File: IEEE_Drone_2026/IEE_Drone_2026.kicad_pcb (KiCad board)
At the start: 4 copper layers, 49 x 49.5 mm, 48 parts, among them IC1 TPSM84209RKHT, J1 ESC, J10 M2, J12 RF, J13 USB_C_Receptacle_USB2.0_16P, J2 M4 Mounting, J3 M4 Mounting, J4 M4 Mounting, J5 M4 Mounting, J6 Pixy2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

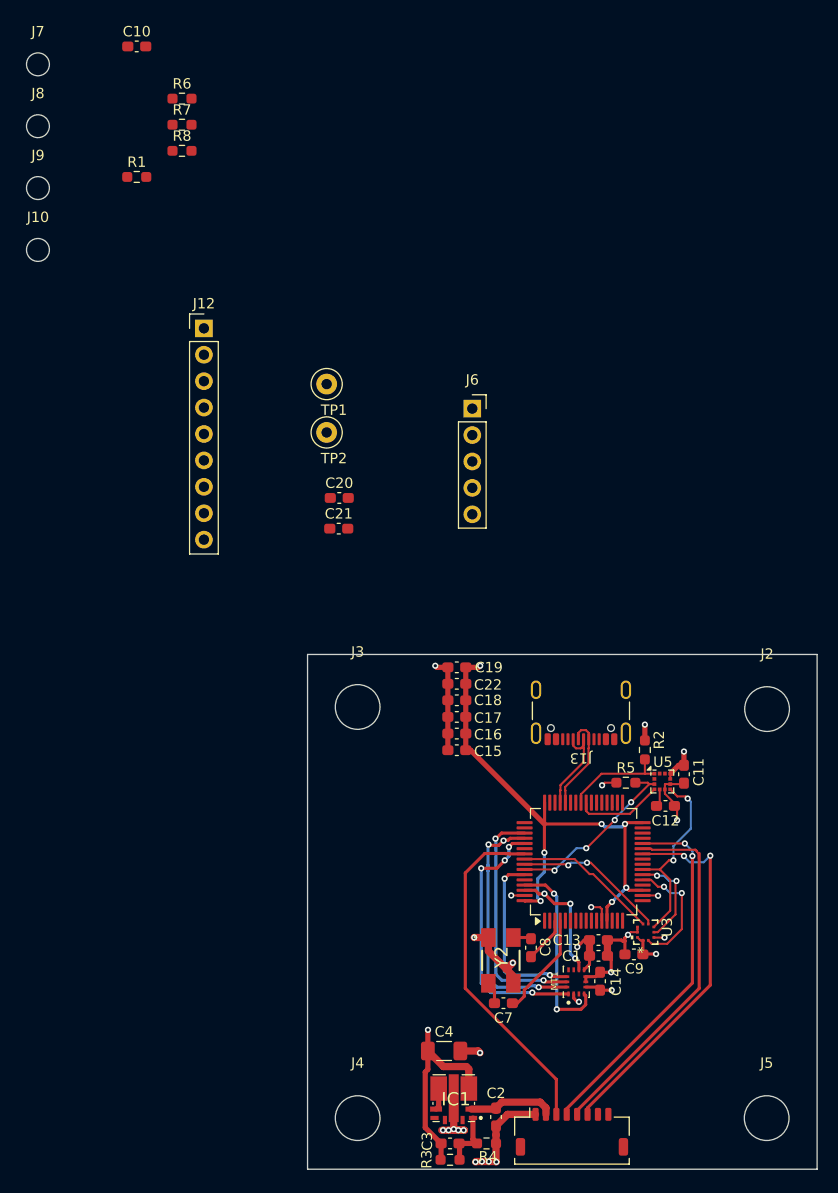
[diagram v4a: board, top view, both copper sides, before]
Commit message: updated lots
finished board internals routing, starting schematic routing for the gps, rf, and pixy
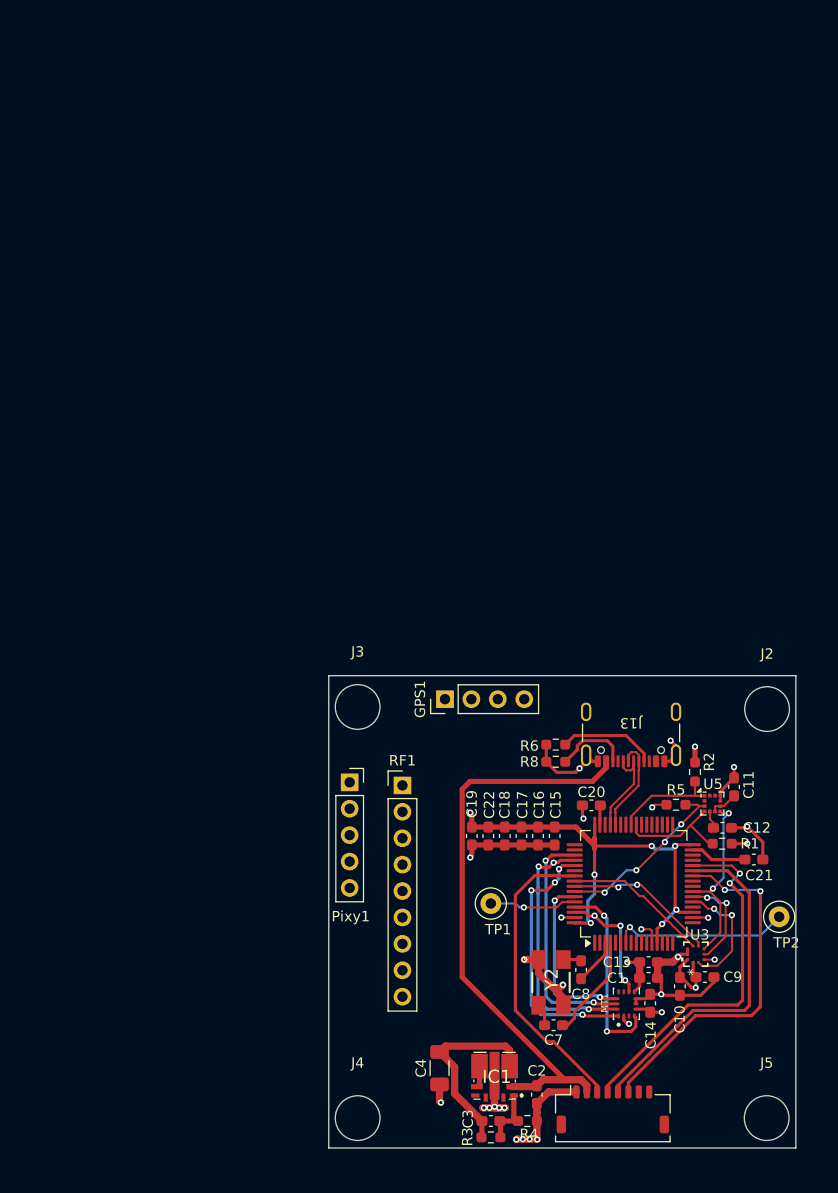
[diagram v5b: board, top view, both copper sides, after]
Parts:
- removed J10, J7, J8, J9: M2, MountingHole:MountingHole_2.2mm_M2
- removed R7: 300, Resistor_SMD:R_0603_1608Metric_Pad0.98x0.95mm_HandSolder
- added GPS1: GPS, Connector_PinHeader_2.54mm:PinHeader_1x04_P2.54mm_Vertical, F.Cu at (76.2, 85.8)
- moved C10 104.4 mm to (98.8, 113.4), turned to -90 degrees
- moved R1 85.3 mm to (102.9, 99.7), turned to 180 degrees
- moved R6 71.8 mm to (86.9, 90.2)
- moved R8 68.9 mm to (86.9, 91.8)
- moved TP2 63.7 mm to (108.3, 106.7)
- moved TP1 52.4 mm to (80.6, 105.5)
- moved C21 51.0 mm to (105.9, 101.2)
- moved RF1 47.9 mm to (72.1, 94.1)
- moved C20 38.2 mm to (90.3, 96.0), turned to 180 degrees
- moved Pixy1 37.8 mm to (67.0, 93.8)
- moved C19 16.3 mm to (78.8, 99.0), turned to -90 degrees
- moved C22 14.9 mm to (80.4, 99.0), turned to -90 degrees
- moved C18 13.8 mm to (82.0, 99.0), turned to -90 degrees
- moved C17 13.0 mm to (83.6, 99.0), turned to -90 degrees
- moved C16 12.6 mm to (85.2, 99.0), turned to -90 degrees
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- renumbered J6 to Pixy1, J12 to RF1
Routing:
- net +VDC: track 8.40 -> 55.6 mm
- net GND: track 58.3 -> 77.8 mm, vias 21 -> 24
- net Net-(U2-NRST): track 0.00 -> 17.1 mm, vias 0 -> 1
- net Net-(J13-CC1): track 0.00 -> 9.41 mm
- net Net-(U2-BOOT0): track 0.00 -> 8.44 mm, vias 0 -> 1
- net Net-(J13-CC2): track 0.00 -> 7.30 mm
- net Net-(U2-VCAP_1): track 0.00 -> 5.40 mm
- net /PB3: track 44.4 -> 40.1 mm
- net /SDA (I2C3): track 8.45 -> 11.3 mm
- net /PB1: track 36.1 -> 33.6 mm
- net Net-(U2-VCAP_2): track 0.00 -> 1.88 mm
- net /PB0: track 36.9 -> 35.3 mm
- net /MOSI: track 18.7 -> 17.4 mm
- net +3.3V: track 89.5 -> 88.3 mm
- net /PB2: track 35.5 -> 35.0 mm
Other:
- board size 49 x 49.5 mm -> 44.9 x 45.4 mm

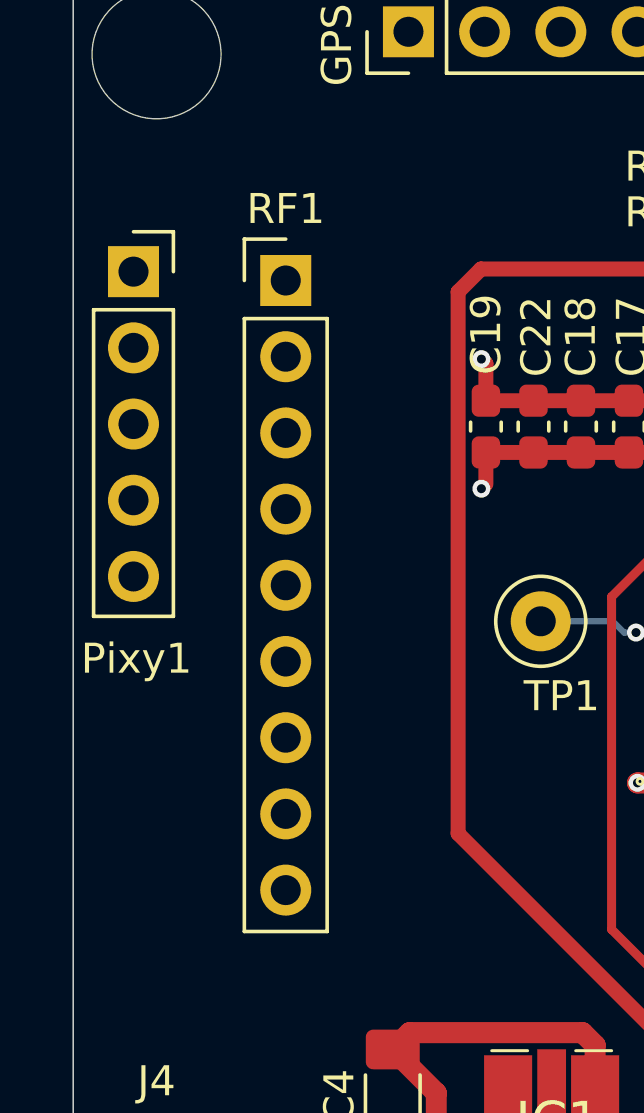
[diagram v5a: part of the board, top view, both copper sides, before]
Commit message: finished schematic connections for pins
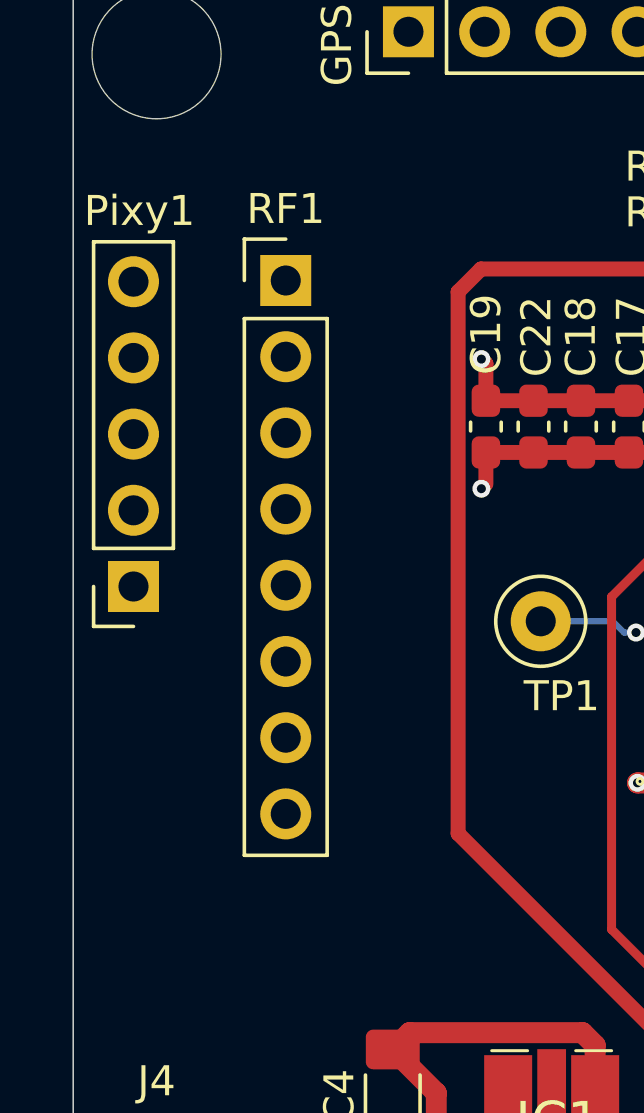
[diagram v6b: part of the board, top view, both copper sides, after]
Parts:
- RF1: footprint Connector_PinHeader_2.54mm:PinHeader_1x09_P2.54mm_Vertical -> Connector_PinHeader_2.54mm:PinHeader_1x08_P2.54mm_Vertical
- moved Pixy1 10.5 mm to (67.0, 104.3), turned to 180 degrees
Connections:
- GPS1 pad 1: unconnected-(GPS1-Pin_1-Pad1) -> +3.3V
- GPS1 pad 2: unconnected-(GPS1-Pin_2-Pad2) -> GND
- GPS1 pad 3: unconnected-(GPS1-Pin_3-Pad3) -> /RX
- GPS1 pad 4: unconnected-(GPS1-Pin_4-Pad4) -> /TX
- Pixy1 pad 1: unconnected-(Pixy1-Pin_1-Pad1) -> /SCK
- Pixy1 pad 2: /SCK -> /MOSI
- Pixy1 pad 3: /MOSI -> /MISO
- Pixy1 pad 4: /MISO -> +VDC
- RF1 pad 1: unconnected-(RF1-Pin_1-Pad1) -> +3.3V
- RF1 pad 2: unconnected-(RF1-Pin_2-Pad2) -> GND
- RF1 pad 3: unconnected-(RF1-Pin_3-Pad3) -> /SCK (SPI3)
- RF1 pad 4: unconnected-(RF1-Pin_4-Pad4) -> /MISO (SPI3)
- RF1 pad 5: unconnected-(RF1-Pin_5-Pad5) -> /MOSI (SPI3)
- RF1 pad 6: unconnected-(RF1-Pin_6-Pad6) -> /PB11
- RF1 pad 7: unconnected-(RF1-Pin_7-Pad7) -> /PB12
- RF1 pad 8: unconnected-(RF1-Pin_8-Pad8) -> /PB13
- U2 pad 14: unconnected-(U2-PA0-Pad14) -> /TX
- U2 pad 15: unconnected-(U2-PA1-Pad15) -> /RX
- U2 pad 30: unconnected-(U2-PB11-Pad30) -> /PB11
- U2 pad 33: unconnected-(U2-PB12-Pad33) -> /PB12
- U2 pad 34: unconnected-(U2-PB13-Pad34) -> /PB13

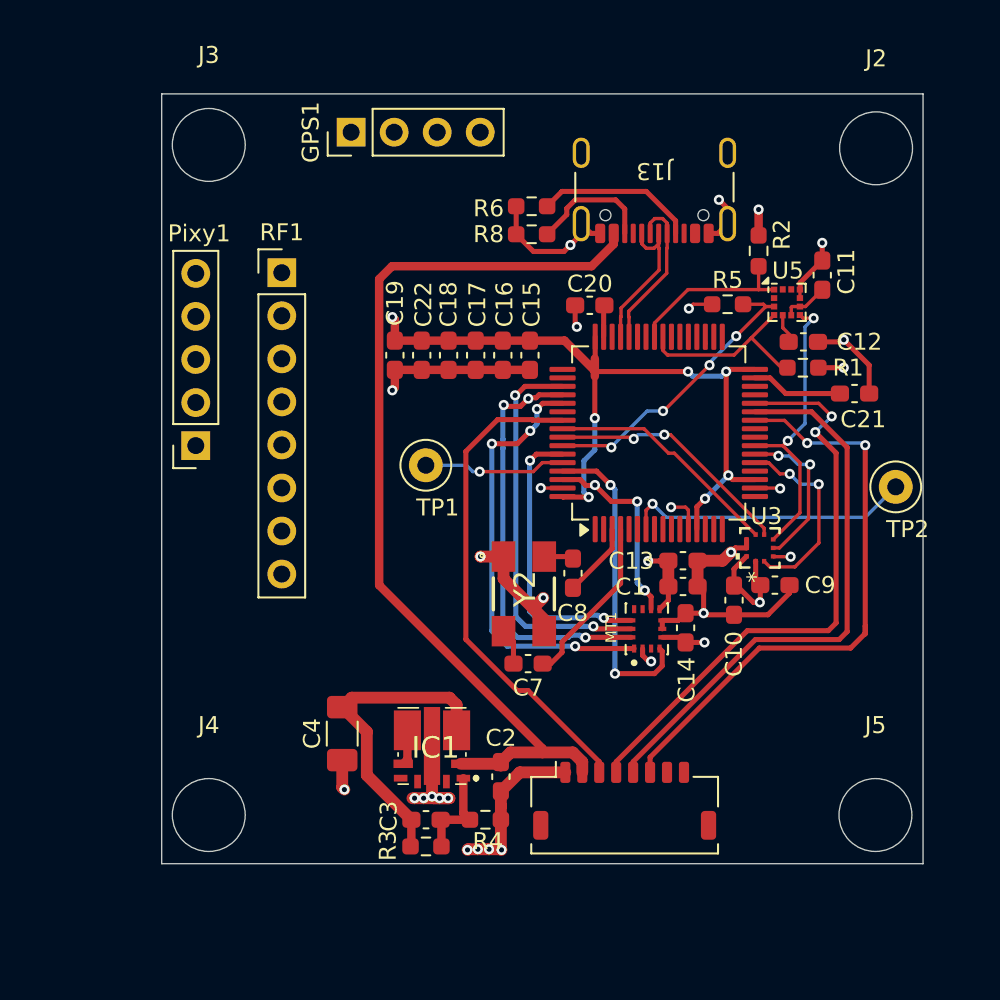
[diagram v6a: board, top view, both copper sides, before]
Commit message: added gnd planes on top and bottom layer
DRC is passing with no errors now
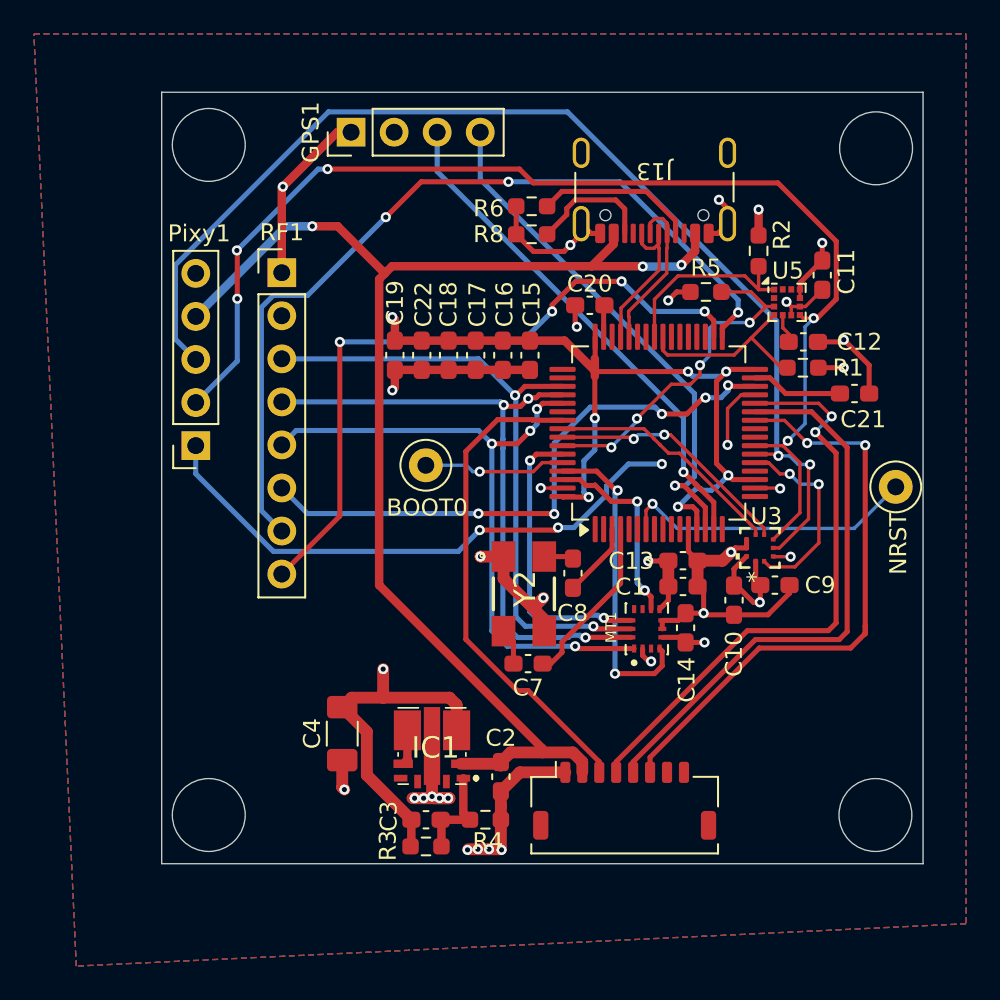
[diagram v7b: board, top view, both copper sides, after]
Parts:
- moved R5 1.47 mm to (97.2, 95.2)
- renumbered TP1 to BOOT0, TP2 to NRST
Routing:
- net /MISO: track 9.55 -> 67.9 mm
- net /MOSI: track 17.4 -> 71.7 mm, vias 2 -> 5
- net /PB12: track 0.00 -> 50.3 mm, vias 0 -> 3
- net /SCK: track 0.00 -> 41.9 mm, vias 0 -> 4
- net /PB13: track 0.00 -> 40.8 mm, vias 0 -> 4
- net /PB11: track 0.00 -> 34.7 mm, vias 0 -> 5
- net /TX: track 0.00 -> 30.5 mm, vias 0 -> 1
- net /RX: track 0.00 -> 30.2 mm, vias 0 -> 1
- net +VDC: track 55.6 -> 77.7 mm, vias 0 -> 3
- net +3.3V: track 88.3 -> 103.1 mm, vias 14 -> 16
- net /SCK (SPI3): track 23.2 -> 37.8 mm
- net /MISO (SPI3): track 24.8 -> 38.0 mm
- net /MOSI (SPI3): track 25.7 -> 38.7 mm
- net /PB6: track 17.5 -> 20.3 mm
- net /SCL (I2C3): track 10.1 -> 11.5 mm
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- added copper zone on B.Cu, net GND
- added copper zone on F.Cu, net GND
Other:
- board size 44.9 x 45.4 mm -> 44.9 x 45.5 mm

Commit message: made prod
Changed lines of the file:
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@@
 		(tags "capacitor handsolder")
 		(property "Reference" "C3"
-			(at -2.1986 -0.2032 90)
+			(at -2.63375 0.135 180)
 			(layer "F.SilkS")
 			(effects
@@
 		(tags "resistor handsolder")
 		(property "Reference" "R3"
-			(at -2.2483 -0.0508 90)
+			(at -2.63265 -0.0508 180)
 			(layer "F.SilkS")
 			(effects
@@
 		(tags "resistor handsolder")
 		(property "Reference" "R4"
-			(at 0.1505 1.27 0)
+			(at 1.11025 1.385 0)
 			(layer "F.SilkS")
 			(effects
@@
 			)
 		)
+	)
+	(zone
+		(net 0)
+		(net_name "")
+		(layer "F.Cu")
+		(hatch edge 0.5)
+		(connect_pads
+			(clearance 0)
+		)
+		(min_thickness 0.25)
+		(filled_areas_thickness no)
+		(keepout
+			(tracks allowed)
+			(vias allowed)
+			(pads allowed)
+			(copperpour not_allowed)
+			(footprints allowed)
+		)
+		(placement
+			(enabled no)
+			(sheetname "/")
+		)
+		(fill
+			(thermal_gap 0.5)
+			(thermal_bridge_width 0.5)
+		)
+		(polygon
+			(pts
+				(xy 68.25 96.25) (xy 71.875 96.75) (xy 72.125 107.75) (xy 67.5 106.75)
+			)
+		)
